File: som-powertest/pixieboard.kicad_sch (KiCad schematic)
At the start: 22 parts, among them J1 Conn_02x20_Counter_Clockwise, J2 Conn_02x20_Counter_Clockwise, J3 Conn_02x20_Counter_Clockwise, J4 Conn_02x20_Counter_Clockwise, J5 Conn_02x20_Counter_Clockwise, J6 Conn_02x20_Counter_Clockwise, J7 Conn_02x20_Counter_Clockwise

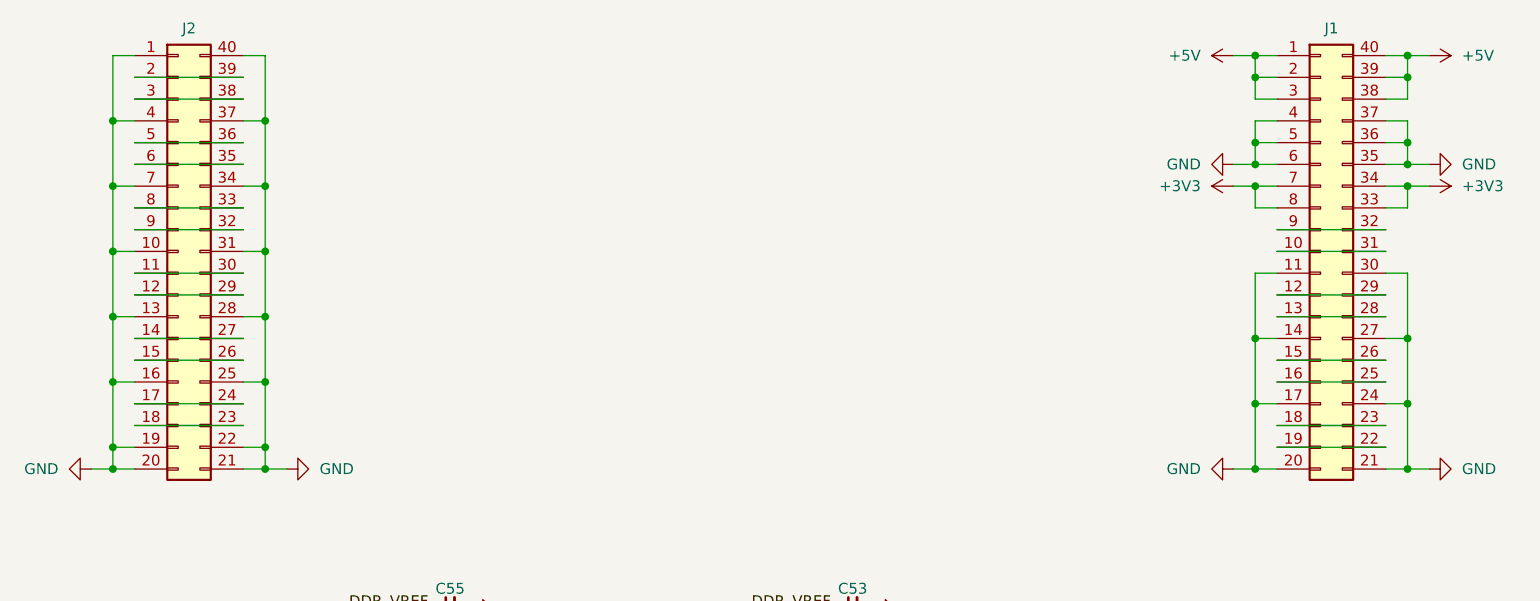
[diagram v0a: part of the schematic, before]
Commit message: Migrate evey power wire off layers in3-in6
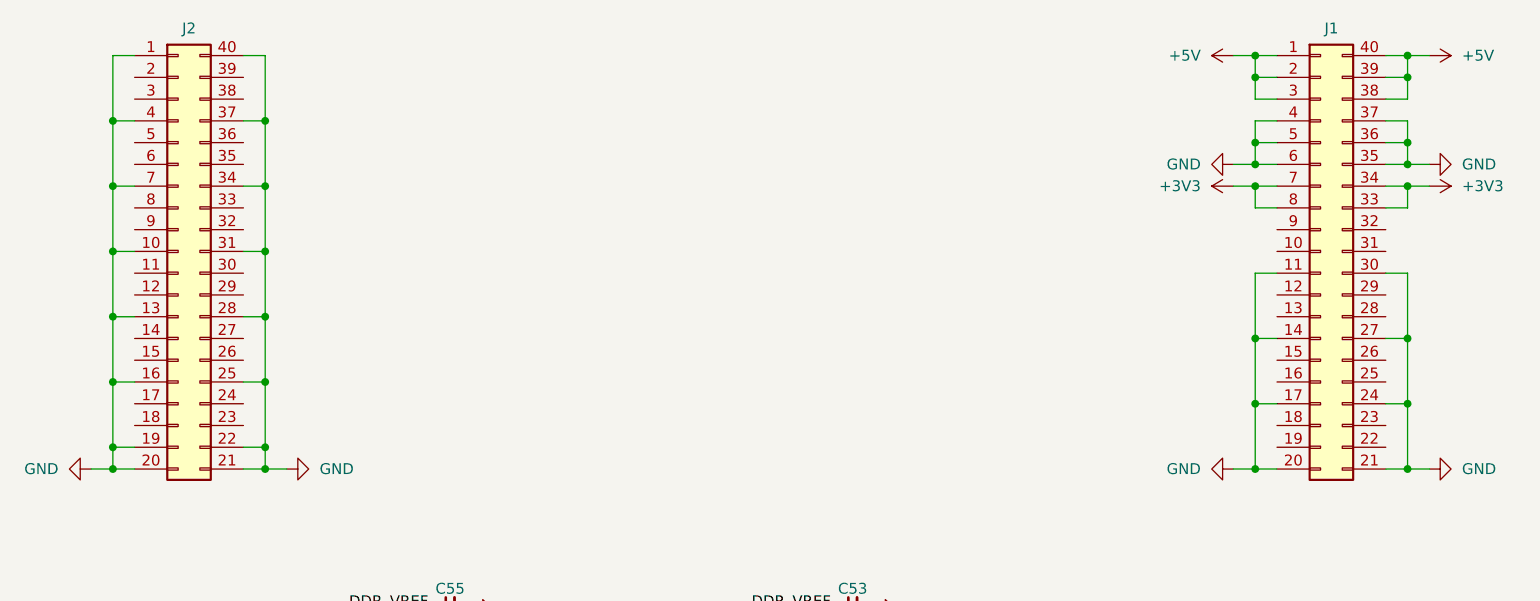
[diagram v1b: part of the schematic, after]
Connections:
- net at J1.10 (Pin_10): no longer J1.31 (Pin_31)
- net at J1.12 (Pin_12): no longer J1.29 (Pin_29)
- net at J1.13 (Pin_13): no longer J1.28 (Pin_28)
- net at J1.15 (Pin_15): no longer J1.26 (Pin_26)
- net at J1.16 (Pin_16): no longer J1.25 (Pin_25)
- net at J1.18 (Pin_18): no longer J1.23 (Pin_23)
- net at J1.19 (Pin_19): no longer J1.22 (Pin_22)
- net at J1.32 (Pin_32): no longer J1.9 (Pin_9)
- net at J2.11 (Pin_11): no longer J2.30 (Pin_30)
- net at J2.12 (Pin_12): no longer J2.29 (Pin_29)
- net at J2.14 (Pin_14): no longer J2.27 (Pin_27)
- net at J2.15 (Pin_15): no longer J2.26 (Pin_26)
- net at J2.17 (Pin_17): no longer J2.24 (Pin_24)
- net at J2.18 (Pin_18): no longer J2.23 (Pin_23)
- net at J2.2 (Pin_2): no longer J2.39 (Pin_39)
- net at J2.3 (Pin_3): no longer J2.38 (Pin_38)
- net at J2.32 (Pin_32): no longer J2.9 (Pin_9)
- net at J2.33 (Pin_33): no longer J2.8 (Pin_8)
- net at J2.35 (Pin_35): no longer J2.6 (Pin_6)
- net at J2.36 (Pin_36): no longer J2.5 (Pin_5)
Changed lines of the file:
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@@
-	(wire
-		(pts
-			(xy 27.94 26.67) (xy 40.64 26.67)
-		)
-		(stroke
-			(width 0)
-			(type default)
-		)
-	)
 	(wire
 		(pts
@@
 	(wire
 		(pts
-			(xy 27.94 54.61) (xy 40.64 54.61)
-		)
-		(stroke
-			(width 0)
-			(type default)
-		)
-	)
-	(wire
-		(pts
 			(xy 173.99 46.99) (xy 176.53 46.99)
 		)
@@
 	(wire
 		(pts
-			(xy 161.29 44.45) (xy 173.99 44.45)
-		)
-		(stroke
-			(width 0)
-			(type default)
-		)
-	)
-	(wire
-		(pts
 			(xy 158.75 46.99) (xy 158.75 54.61)
 		)
@@
 	(wire
 		(pts
-			(xy 161.29 64.77) (xy 173.99 64.77)
-		)
-		(stroke
-			(width 0)
-			(type default)
-		)
-	)
-	(wire
-		(pts
 			(xy 237.49 388.62) (xy 242.57 388.62)
 		)
@@
 	(wire
 		(pts
-			(xy 27.94 39.37) (xy 40.64 39.37)
-		)
-		(stroke
-			(width 0)
-			(type default)
-		)
-	)
-	(wire
-		(pts
 			(xy 158.75 36.83) (xy 158.75 39.37)
 		)
@@
 	(wire
 		(pts
-			(xy 27.94 46.99) (xy 40.64 46.99)
-		)
-		(stroke
-			(width 0)
-			(type default)
-		)
-	)
-	(wire
-		(pts
 			(xy 158.75 62.23) (xy 161.29 62.23)
 		)
@@
 	(wire
 		(pts
-			(xy 161.29 41.91) (xy 173.99 41.91)
-		)
-		(stroke
-			(width 0)
-			(type default)
-		)
-	)
-	(wire
-		(pts
 			(xy 156.21 21.59) (xy 158.75 21.59)
 		)
@@
 	(wire
 		(pts
-			(xy 27.94 31.75) (xy 40.64 31.75)
-		)
-		(stroke
-			(width 0)
-			(type default)
-		)
-	)
-	(wire
-		(pts
 			(xy 166.37 201.93) (xy 166.37 204.47)
 		)
@@
 	(wire
 		(pts
-			(xy 27.94 57.15) (xy 40.64 57.15)
-		)
-		(stroke
-			(width 0)
-			(type default)
-		)
-	)
-	(wire
-		(pts
 			(xy 25.4 59.69) (xy 27.94 59.69)
 		)
@@
 	(wire
 		(pts
-			(xy 161.29 52.07) (xy 173.99 52.07)
-		)
-		(stroke
-			(width 0)
-			(type default)
-		)
-	)
-	(wire
-		(pts
 			(xy 242.57 388.62) (xy 255.27 388.62)
 		)
@@
 	(wire
 		(pts
-			(xy 27.94 49.53) (xy 40.64 49.53)
-		)
-		(stroke
-			(width 0)
-			(type default)
-		)
-	)
-	(wire
-		(pts
-			(xy 161.29 59.69) (xy 173.99 59.69)
-		)
-		(stroke
-			(width 0)
-			(type default)
-		)
-	)
-	(wire
-		(pts
 			(xy 257.81 381) (xy 255.27 381)
 		)
@@
 	(wire
 		(pts
-			(xy 27.94 24.13) (xy 40.64 24.13)
-		)
-		(stroke
-			(width 0)
-			(type default)
-		)
-	)
-	(wire
-		(pts
 			(xy 25.4 52.07) (xy 25.4 59.69)
 		)
@@
 	(wire
 		(pts
-			(xy 27.94 34.29) (xy 40.64 34.29)
-		)
-		(stroke
-			(width 0)
-			(type default)
-		)
-	)
-	(wire
-		(pts
 			(xy 158.75 54.61) (xy 161.29 54.61)
 		)
@@
 	(wire
 		(pts
-			(xy 27.94 41.91) (xy 40.64 41.91)
-		)
-		(stroke
-			(width 0)
-			(type default)
-		)
-	)
-	(wire
-		(pts
 			(xy 240.03 396.24) (xy 240.03 391.16)
 		)
@@
 	(wire
 		(pts
-			(xy 161.29 49.53) (xy 173.99 49.53)
-		)
-		(stroke
-			(width 0)
-			(type default)
-		)
-	)
-	(wire
-		(pts
 			(xy 40.64 69.85) (xy 43.18 69.85)
 		)
@@
 	(wire
 		(pts
-			(xy 161.29 67.31) (xy 173.99 67.31)
-		)
-		(stroke
-			(width 0)
-			(type default)
-		)
-	)
-	(wire
-		(pts
 			(xy 158.75 62.23) (xy 158.75 69.85)
 		)
@@
 	(wire
 		(pts
-			(xy 27.94 62.23) (xy 40.64 62.23)
-		)
-		(stroke
-			(width 0)
-			(type default)
-		)
-	)
-	(wire
-		(pts
 			(xy 22.86 69.85) (xy 25.4 69.85)
 		)
@@
 	(wire
 		(pts
-			(xy 161.29 57.15) (xy 173.99 57.15)
-		)
-		(stroke
-			(width 0)
-			(type default)
-		)
-	)
-	(wire
-		(pts
 			(xy 176.53 39.37) (xy 173.99 39.37)
 		)
 		(stroke
-			(width 0)
-			(type default)
-		)
-	)
-	(wire
-		(pts
-			(xy 27.94 64.77) (xy 40.64 64.77)
-		)
-		(stroke
